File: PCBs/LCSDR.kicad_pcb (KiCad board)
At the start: 2 copper layers, 70 x 100 mm, 110 parts, among them CON2 AVR-ISP-6, J1 MIC, J10 SPK, J12 Conn_01x01, J13 Conn_01x01, J14 Conn_01x01, J15 Conn_01x01, J2 ANT, J3 USB_B, J4 CAL, J5 MEASURE, J6 I2C, J7 MEASURE, J8 Jack-DC, K1 TIANBO-HJR-4102-L, Q1 2N7002, Q2 2N7002, Q3 BC847, Q4 BS170, Q6 BS170, Q7 BF998, Q8 BS170, Q9 BC849, U1 74AC14, U2 Si5351, U3 FT232RL, U4 LM1117-5.0, U5 LM1117-3.3, U6 ATMEGA328P-AU, Y1 25Mhz, Y2 20Mhz

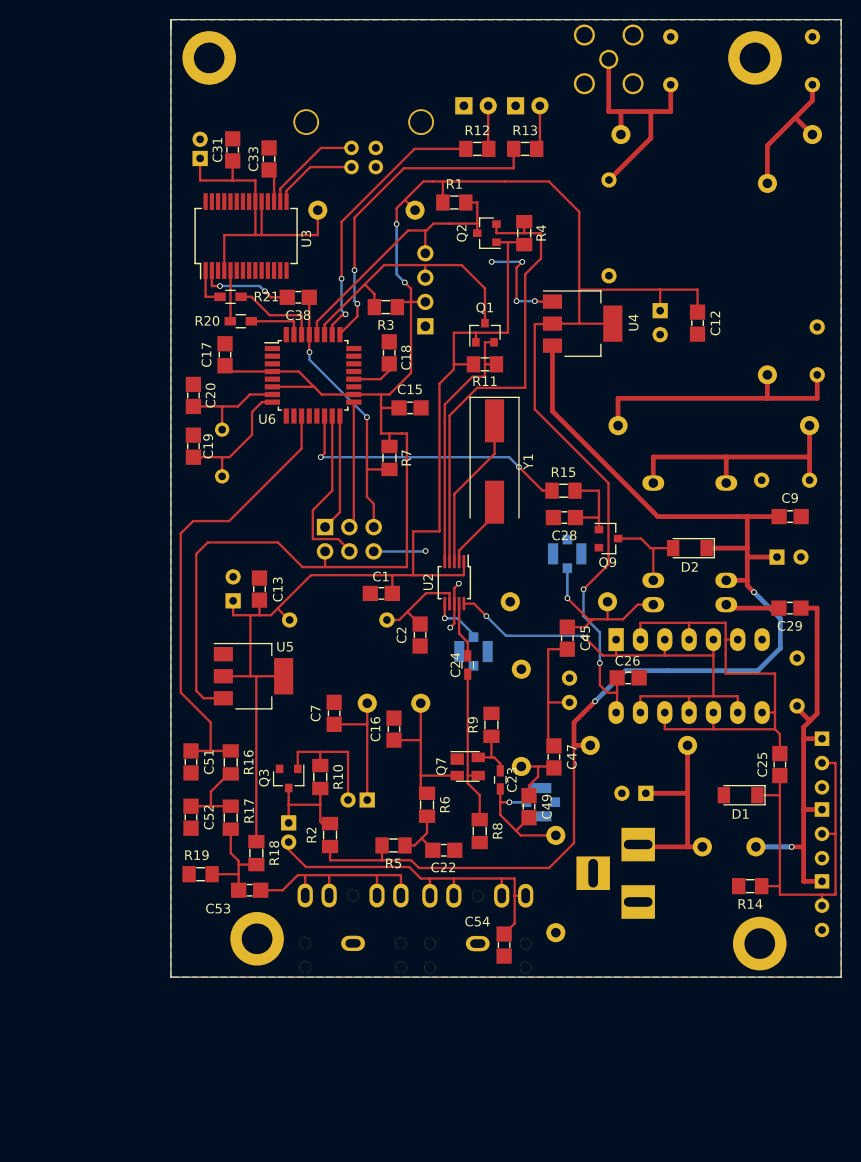
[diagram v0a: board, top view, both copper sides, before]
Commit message: ADX988 CAT: add FE, FI commands
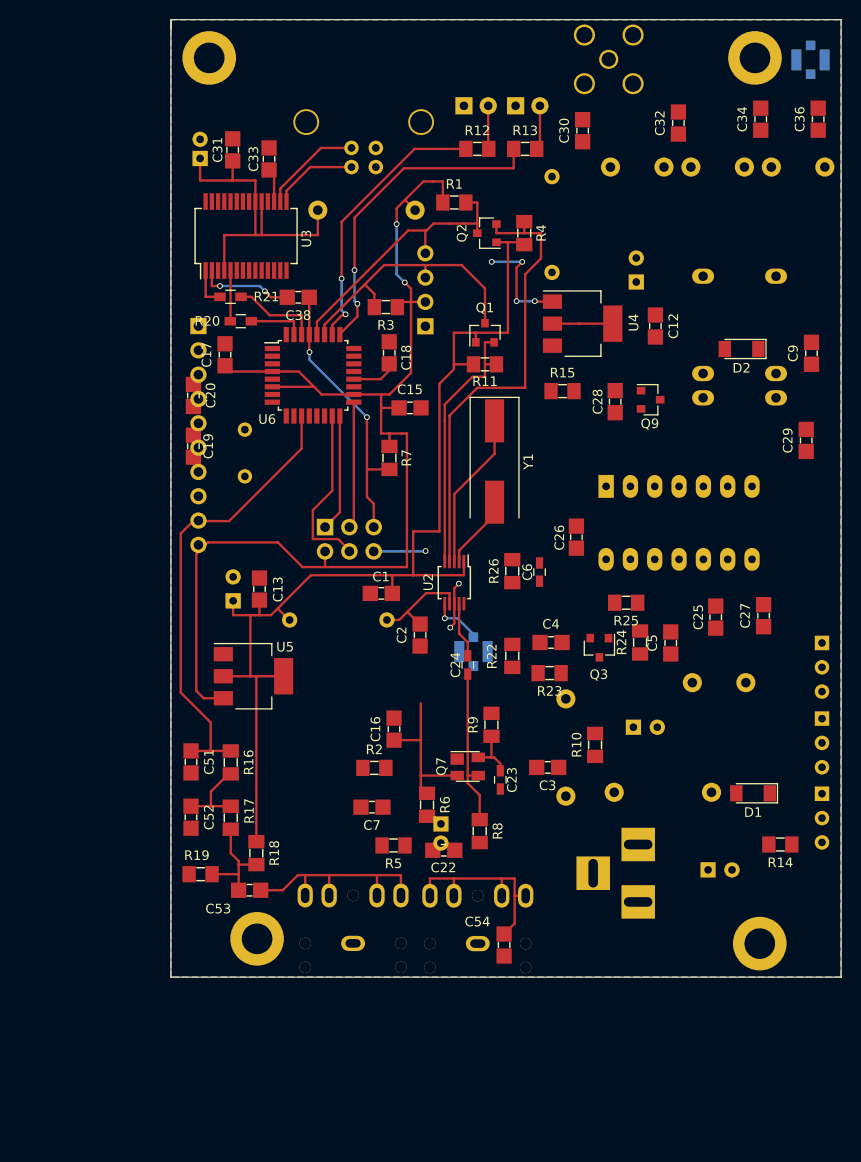
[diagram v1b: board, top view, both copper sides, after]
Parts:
- removed C45, C49: 330pF, LCSDR:C_1206_0603
- removed C47: 220pF, LCSDR:C_1206_0603
- removed L13, L19: 1uH, Choke_Axial_ThroughHole:Choke_Horizontal_RM10mm
- removed L15: 680nH, Resistors_THT:R_Axial_DIN0309_L9.0mm_D3.2mm_P2.54mm_Vertical
- removed L17: 680nH, Choke_Axial_ThroughHole:Choke_Horizontal_RM10mm
- removed L4: 100mH, Choke_Toroid_ThroughHole:Choke_Toroid_6,5x13mm_Vertical
- added C4: 100nF, LCSDR:C_1206_0603, F.Cu at (139.7, 125.0)
- added C5: 100nF, LCSDR:C_1206_0603, F.Cu at (152.2, 125.1)
- added C6: 10nF, Capacitors_SMD:C_0603_HandSoldering, F.Cu at (138.5, 117.7)
- added L3: 5.6uH, Choke_Axial_ThroughHole:Choke_Horizontal_RM10mm, B.Cu at (141.2, 136.1)
- added R22: 4.7, LCSDR:R_1206_0603, F.Cu at (135.7, 126.5)
- added R23: 47, LCSDR:R_1206_0603, F.Cu at (139.6, 128.2)
- added R24: 2.7K, LCSDR:R_1206_0603, F.Cu at (149.0, 125.0)
- added R25: 470, LCSDR:R_1206_0603, F.Cu at (147.6, 120.9)
- added R26: 1K, LCSDR:R_1206_0603, F.Cu at (135.7, 117.6)
- C16, C7: value 100nF -> 10nF
- C27: footprint Capacitors_THT:C_Disc_D4.7mm_W2.5mm_P5.00mm -> LCSDR:C_1206_0603; moved to F.Cu
- C3: value 2.2uF -> 100nF; footprint Capacitors_THT:CP_Radial_D5.0mm_P2.00mm -> LCSDR:C_1206_0603; moved to F.Cu
- C30, C36: value 270pF -> 360pF; footprint Capacitors_THT:C_Disc_D4.7mm_W2.5mm_P5.00mm -> LCSDR:C_1206_0603; moved to F.Cu
- C32, C34: value 680pF -> 750pF; footprint Capacitors_THT:C_Disc_D4.7mm_W2.5mm_P5.00mm -> LCSDR:C_1206_0603; moved to F.Cu
- J5: value MEASURE -> LPF
- J7: value MEASURE -> Conn_01x10; footprint LCSDR:U.FL_Molex_MCRF_73412-0110_Vertical -> Pin_Headers:Pin_Header_Straight_1x10_Pitch2.54mm
- L10, L6: value 1.32uH -> 1.22uH; footprint Choke_Axial_ThroughHole:Choke_Horizontal_RM20mm -> Choke_Toroid_ThroughHole:Choke_Toroid_6,5x13mm_Vertical
- L8: value 1.72uH -> 1.42uH; footprint Choke_Axial_ThroughHole:Choke_Horizontal_RM20mm -> Choke_Toroid_ThroughHole:Choke_Toroid_6,5x13mm_Vertical
- Q3: value BC847 -> BFR93A
- R10: value 470k -> 33
- R2: value 3.9K -> 2.2K
- moved J7 61.3 mm to (102.9, 92.0), turned to 180 degrees
- moved J5 57.5 mm to (166.8, 64.2), turned to 0 degrees
- moved C36 37.7 mm to (167.6, 70.4), turned to 90 degrees
- moved Q3 35.2 mm to (144.8, 125.6)
- moved R10 28.9 mm to (144.3, 135.8), turned to 90 degrees
- moved C3 27.7 mm to (139.3, 138.1), turned to 180 degrees
- moved C34 27.3 mm to (161.6, 70.4)
- moved C8 23.3 mm to (148.3, 133.9)
- moved K1 22.2 mm to (163.2, 86.8)
- moved D2 21.5 mm to (159.6, 94.4)
- moved L10 21.1 mm to (162.2, 82.0), turned to 90 degrees
- moved C29 17.6 mm to (166.3, 104.0), turned to 90 degrees
- moved C9 17.2 mm to (166.9, 94.8), turned to 90 degrees
- moved L5 17.2 mm to (153.9, 135.8)
- moved C25 16.8 mm to (156.9, 122.4)
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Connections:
- C23 pad 2: HPF -> Net-(C23-Pad2)
- C3 pad 2: Net-(C3-Pad2) -> GND
- C54 pad 1: Net-(C3-Pad2) -> Net-(C14-Pad2)
- J1 pad 2: Net-(C3-Pad2) -> Net-(C14-Pad2)
- J1 pad 3: Net-(C3-Pad2) -> Net-(C14-Pad2)
- J1 pad 4: Net-(C3-Pad2) -> Net-(C14-Pad2)
- J1 pad 5: Net-(C3-Pad2) -> Net-(C14-Pad2)
- J3 pad 1: (no net) -> Net-(J3-Pad1)
- J5 pad 1: RF_IN -> LPF
- J7 pad 1: HPF -> GND
- J7 pad 2: GND -> IO_4
- Q3 pad 1: Net-(C14-Pad2) -> Net-(C6-Pad1)
- Q3 pad 2: GND -> Net-(C4-Pad2)
- Q3 pad 3: Net-(C3-Pad1) -> Net-(C23-Pad2)
- R10 pad 1: Net-(C14-Pad2) -> Net-(C3-Pad1)
- R10 pad 2: Net-(C3-Pad1) -> +12V
- R2 pad 1: +12V -> Net-(C16-Pad1)
- R2 pad 2: Net-(C3-Pad1) -> Net-(C14-Pad1)
- U3 pad 10: (no net) -> Net-(U3-Pad10)
- U3 pad 11: (no net) -> Net-(U3-Pad11)
- U3 pad 12: (no net) -> Net-(U3-Pad12)
- U3 pad 13: (no net) -> Net-(U3-Pad13)
- U3 pad 14: (no net) -> Net-(U3-Pad14)
- U3 pad 22: (no net) -> Net-(U3-Pad22)
- U3 pad 23: (no net) -> Net-(U3-Pad23)
- U3 pad 27: (no net) -> Net-(U3-Pad27)
- U3 pad 28: (no net) -> Net-(U3-Pad28)
- U3 pad 3: (no net) -> Net-(U3-Pad3)
- U3 pad 6: (no net) -> Net-(U3-Pad6)
- U3 pad 9: (no net) -> Net-(U3-Pad9)
- U6 pad 1: (no net) -> IO_5
- U6 pad 12: (no net) -> IO_8
- U6 pad 13: (no net) -> IO_9
- U6 pad 14: RX_TX -> IO_10
- U6 pad 19: (no net) -> Net-(U6-Pad19)
- U6 pad 2: (no net) -> IO_6
- U6 pad 22: (no net) -> Net-(U6-Pad22)
- U6 pad 23: (no net) -> RX_TX
- U6 pad 24: (no net) -> IO_1
- U6 pad 32: (no net) -> IO_4
- U6 pad 9: (no net) -> IO_7
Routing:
- net +12V: track 128.7 -> 0.00 mm, vias 2 -> 0
- net +5V: track 224.0 -> 162.5 mm, vias 4 -> 2
- net CLK0: track 52.8 -> 0.00 mm, vias 2 -> 0
- net Net-(C25-Pad1): track 49.0 -> 0.00 mm
- net Net-(C27-Pad1): track 43.7 -> 0.00 mm, vias 1 -> 0
- net Net-(C25-Pad2): track 40.2 -> 0.00 mm
- net Net-(C3-Pad2): track 38.4 -> 0.00 mm
- net Net-(C51-Pad1): track 47.8 -> 14.9 mm
- net RX_TX: track 30.1 -> 0.00 mm, vias 2 -> 0
- net Net-(C34-Pad1): track 28.6 -> 0.00 mm
- net LPF: track 27.5 -> 0.00 mm
- net Net-(C30-Pad1): track 26.1 -> 0.00 mm
- net +12VA: track 21.8 -> 0.35 mm
- net RF_IN: track 18.5 -> 0.00 mm, vias 1 -> 0
- net Net-(C32-Pad1): track 14.8 -> 0.00 mm
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
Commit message: discret, simple, CH340E
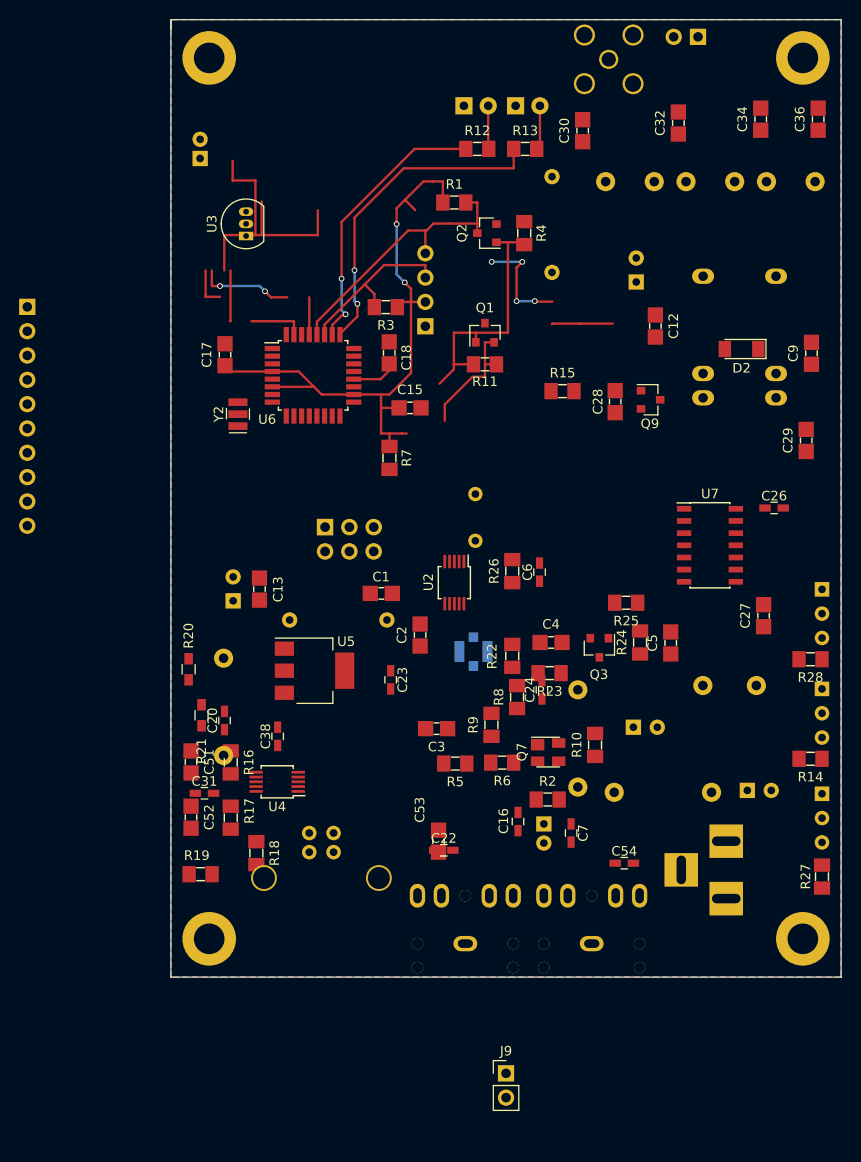
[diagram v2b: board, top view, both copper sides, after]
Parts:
- removed C19: 22pF, LCSDR:C_1206_0603
- removed C25, C33: 100nF, LCSDR:C_1206_0603
- removed D1: LL4148, Diodes_SMD:D_MiniMELF
- removed L12: 10uH, Choke_Axial_ThroughHole:Choke_Horizontal_RM10mm
- removed U1: 74AC14, Housings_DIP:DIP-14_W7.62mm_LongPads
- added J9: Conn_01x02, Pin_Headers:Pin_Header_Straight_1x02_Pitch2.54mm, F.Cu at (135.0, 170.1)
- added L4: 10uH, Choke_Axial_ThroughHole:Choke_Horizontal_RM10mm, B.Cu at (105.5, 131.8)
- added R27: 1R, LCSDR:R_1206_0603, F.Cu at (168.0, 149.5)
- added R28: 1R, LCSDR:R_1206_0603, F.Cu at (166.8, 126.8)
- added U7: 74ACT00, Housings_SOIC:SOIC-14_3.9x8.7mm_Pitch1.27mm, F.Cu at (156.3, 114.9)
- C16, C22, C26, C31, C38, C54, C7: footprint LCSDR:C_1206_0603 -> Capacitors_SMD:C_0603_HandSoldering
- C20: value 22pF -> 100nF; footprint LCSDR:C_1206_0603 -> Capacitors_SMD:C_0603_HandSoldering
- J5: value LPF -> Conn_01x02; footprint LCSDR:U.FL_Molex_MCRF_73412-0110_Vertical -> Pin_Headers:Pin_Header_Straight_1x02_Pitch2.54mm
- L10, L6, L8: footprint Choke_Toroid_ThroughHole:Choke_Toroid_6,5x13mm_Vertical -> Choke_Toroid_ThroughHole:Choke_Toroid_5x10mm_Vertical
- R14: value 2.7K -> 1R
- U3: value FT232RL -> L78L05_TO92; footprint Housings_SSOP:SSOP-28_5.3x10.2mm_Pitch0.65mm -> TO_SOT_Packages_THT:TO-92_Inline_Narrow_Oval
- U4: value LM1117-5.0 -> CH340E; footprint TO_SOT_Packages_SMD:SOT-223-3_TabPin2 -> Housings_SSOP:MSOP-10_3x3mm_Pitch0.5mm
- Y1: footprint Crystals:Crystal_SMD_HC49-SD -> Crystals:Crystal_HC49-U_Vertical; moved to B.Cu
- Y2: value 20Mhz -> 16Mhz; footprint Crystals:Crystal_HC49-U_Vertical -> LCSDR:Crystal_SMD_3213_3.2x1.3mm; moved to F.Cu
- moved J3 69.9 mm to (114.5, 144.9), turned to 270 degrees
- moved C31 67.3 mm to (103.5, 140.8), turned to 0 degrees
- moved U4 57.5 mm to (111.1, 139.6), turned to 180 degrees
- moved C38 45.9 mm to (111.2, 134.8), turned to 90 degrees
- moved R21 43.8 mm to (103.2, 132.7), turned to 90 degrees
- moved R20 36.8 mm to (101.8, 127.8), turned to 90 degrees
- moved C20 34.1 mm to (105.6, 133.2)
- moved C7 21.0 mm to (141.8, 144.9), turned to 270 degrees
- moved C26 20.9 mm to (163.0, 111.0), turned to 0 degrees
- moved C53 20.4 mm to (128.0, 145.8), turned to 90 degrees
- moved R2 18.4 mm to (139.3, 141.4)
- moved J7 18.0 mm to (85.0, 90.0)
- moved C16 16.2 mm to (136.2, 143.8), turned to 270 degrees
- moved C23 15.5 mm to (123.0, 128.9)
- moved C54 15.2 mm to (147.3, 148.1), turned to 0 degrees
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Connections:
- C31 pad 1: Net-(C31-Pad1) -> GND
- C31 pad 2: GND -> Net-(C31-Pad2)
- C38 pad 1: RESET -> Net-(C38-Pad1)
- C38 pad 2: Net-(C38-Pad2) -> RESET
- C44 pad 1: Net-(C31-Pad1) -> Net-(C20-Pad1)
- J3 pad 1: Net-(J3-Pad1) -> (no net)
- J5 pad 1: LPF -> Net-(C30-Pad1)
- Q1 pad 2: Net-(Q1-Pad2) -> SCL
- Q1 pad 3: SDA -> Net-(Q1-Pad3)
- Q2 pad 2: Net-(Q2-Pad2) -> SDA
- Q2 pad 3: SCL -> Net-(Q2-Pad3)
- Q4 pad 2: Net-(C25-Pad2) -> Net-(Q4-Pad2)
- Q4 pad 3: GND -> Net-(Q4-Pad3)
- Q6 pad 2: Net-(C25-Pad2) -> Net-(Q4-Pad2)
- Q6 pad 3: GND -> Net-(Q6-Pad3)
- Q8 pad 2: Net-(C25-Pad2) -> Net-(Q4-Pad2)
- Q8 pad 3: GND -> Net-(Q8-Pad3)
- R11 pad 2: Net-(Q1-Pad2) -> Net-(Q2-Pad3)
- R14 pad 1: Net-(C25-Pad2) -> Net-(Q4-Pad3)
- R20 pad 1: TxD -> Net-(R20-Pad1)
- R20 pad 2: Net-(R20-Pad2) -> TxD
- R21 pad 1: RxD -> Net-(R21-Pad1)
- R21 pad 2: Net-(R21-Pad2) -> RxD
- R4 pad 2: Net-(Q2-Pad2) -> Net-(Q1-Pad3)
- U2 pad 4: Net-(Q2-Pad2) -> Net-(Q1-Pad3)
- U2 pad 5: Net-(Q1-Pad2) -> Net-(Q2-Pad3)
- U3 pad 1: Net-(R21-Pad2) -> +5V
- U3 pad 2: Net-(C38-Pad2) -> GND
- U3 pad 3: Net-(U3-Pad3) -> +12V
- U4 pad 1: GND -> Net-(J3-Pad3)
- U4 pad 2: +5V -> Net-(J3-Pad2)
- U4 pad 3: +12V -> GND
- U5 pad 3: +5V -> +12V
- U6 pad 19: Net-(U6-Pad19) -> (no net)
- U6 pad 22: Net-(U6-Pad22) -> (no net)
- U6 pad 24: IO_1 -> (no net)
- U6 pad 7: Net-(C20-Pad1) -> Net-(U6-Pad7)
- Y2 pad 2: Net-(C20-Pad1) -> GND
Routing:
- net +5V: track 162.5 -> 66.6 mm
- net +3V3: track 113.9 -> 27.2 mm
- net (no net): track 0.00 -> 67.1 mm, vias 0 -> 6
- net Net-(Q2-Pad2): track 48.0 -> 0.00 mm
- net Net-(C31-Pad1): track 35.4 -> 0.00 mm
- net Net-(Q1-Pad2): track 27.6 -> 0.00 mm
- net RESET: track 29.1 -> 3.90 mm, vias 2 -> 0
- net Net-(C53-Pad1): track 23.8 -> 0.00 mm
- net GND: track 21.9 -> 0.00 mm, vias 7 -> 0
- net Net-(C14-Pad2): track 21.7 -> 0.00 mm
- net Net-(U2-Pad3): track 19.2 -> 0.00 mm
- net Net-(CON2-Pad4): track 18.1 -> 0.00 mm
- net Net-(C24-Pad1): track 16.8 -> 0.00 mm
- net Net-(C16-Pad1): track 16.3 -> 0.00 mm
- net Net-(C51-Pad1): track 14.9 -> 0.00 mm
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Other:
- net class Default: trace_width 0.25 -> 0.2

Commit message: INIT project, si5351 generate properly frequency
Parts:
- removed C17, C18: 100nF, LCSDR:C_1206_0603
- removed C20, C31, C38: 100nF, Capacitors_SMD:C_0603_HandSoldering
- removed C44: 10uF, Capacitors_THT:CP_Radial_D5.0mm_P2.00mm
- removed CON2: AVR-ISP-6, Connectors_IDC:IDC-Header_2x03_Pitch2.54mm_Straight
- removed J3: USB_B, Connectors:USB_B
- removed J6: I2C, Pin_Headers:Pin_Header_Straight_1x04_Pitch2.54mm
- removed L4: 10uH, Choke_Axial_ThroughHole:Choke_Horizontal_RM10mm
- removed R20, R21: 1K, Resistors_SMD:R_0603_HandSoldering
- removed R7: 10k, LCSDR:R_1206_0603
- removed U3: L78L05_TO92, TO_SOT_Packages_THT:TO-92_Inline_Narrow_Oval
- removed U4: CH340E, Housings_SSOP:MSOP-10_3x3mm_Pitch0.5mm
- removed Y2: 16Mhz, LCSDR:Crystal_SMD_3213_3.2x1.3mm
- added U1: 24LC01, Housings_SOIC:SOIC-8_3.9x4.9mm_Pitch1.27mm, F.Cu at (115.9, 154.3)
- C12, C13, C15, C29, C3, C30, C32, C34, C36, C4, C5, C51, C52, C9: footprint LCSDR:C_1206_0603 -> Capacitors_SMD:C_0603_HandSoldering
- C27: value 100pF -> 100nF; footprint LCSDR:C_1206_0603 -> Capacitors_SMD:C_0603_HandSoldering
- C28: value 100pF -> 15nF; footprint LCSDR:C_1206_0603 -> Capacitors_SMD:C_0603_HandSoldering
- C53: value 100nF -> 1uF; footprint LCSDR:C_1206_0603 -> Capacitors_SMD:C_0603_HandSoldering
- D3, D4: footprint LEDs:LED_D3.0mm_Horizontal_O3.81mm_Z10.0mm -> LEDs:LED_0603_HandSoldering
- J9: moved to B.Cu
- L1: footprint Resistors_THT:R_Axial_DIN0207_L6.3mm_D2.5mm_P10.16mm_Horizontal -> Choke_Axial_ThroughHole:Choke_Horizontal_RM10mm
- L10, L6: value 1.22uH -> 1.42uH
- L8: value 1.42uH -> 1.62uH
- R1, R11, R15, R16, R17, R18, R19, R3, R4: footprint LCSDR:R_1206_0603 -> Resistors_SMD:R_0603_HandSoldering
- R12, R13: footprint LCSDR:R_1206_0603 -> Resistors_SMD:R_0603_HandSoldering; moved to B.Cu
- U6: value ATMEGA328P-AU -> Arduino_Nano; footprint Housings_QFP:TQFP-32_7x7mm_Pitch0.8mm -> Arduino:Arduino_Nano; moved to B.Cu
- moved J9 69.6 mm to (141.5, 100.8), turned to 270 degrees
- moved J7 62.1 mm to (102.6, 149.6), turned to 0 degrees
- moved Q2 59.5 mm to (117.0, 139.7), turned to 0 degrees
- moved C15 58.5 mm to (114.2, 158.1)
- moved C10 56.6 mm to (103.6, 121.8)
- moved C12 56.4 mm to (106.6, 127.2), turned to 90 degrees
- moved R1 55.1 mm to (113.8, 131.9)
- moved R4 48.7 mm to (118.3, 127.3), turned to 0 degrees
- moved J2 47.2 mm to (119.0, 103.2)
- moved J5 47.2 mm to (128.5, 100.8)
- moved R3 46.8 mm to (113.1, 135.8), turned to 270 degrees
- moved E1 45.3 mm to (111.4, 111.7), turned to 180 degrees
- moved C30 43.9 mm to (124.7, 111.5), turned to 0 degrees
- moved R11 43.8 mm to (117.0, 136.8)
- moved R13 41.6 mm to (108.7, 104.0), turned to 90 degrees
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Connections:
- C51 pad 1: Net-(C51-Pad1) -> AUDIO_IN
- R16 pad 1: Net-(C51-Pad1) -> AUDIO_IN
- U6 pad 1: IO_5 -> (no net)
- U6 pad 10: GND -> AUDIO_IN
- U6 pad 11: Net-(C51-Pad1) -> IO_6
- U6 pad 12: IO_8 -> IO_5
- U6 pad 13: IO_9 -> IO_4
- U6 pad 14: IO_10 -> (no net)
- U6 pad 15: Net-(CON2-Pad4) -> (no net)
- U6 pad 16: Net-(CON2-Pad1) -> (no net)
- U6 pad 17: Net-(CON2-Pad3) -> (no net)
- U6 pad 18: +5V -> (no net)
- U6 pad 19: (no net) -> IO_7
- U6 pad 2: IO_6 -> (no net)
- U6 pad 20: Net-(C18-Pad1) -> IO_8
- U6 pad 21: GND -> IO_9
- U6 pad 22: (no net) -> IO_10
- U6 pad 23: RX_TX -> SDA
- U6 pad 24: (no net) -> SCL
- U6 pad 25: LED_RED -> AUDIO_IN
- U6 pad 26: LED_GREEN -> AUDIO_IN
- U6 pad 27: SDA -> +5V
- U6 pad 28: SCL -> (no net)
- U6 pad 29: RESET -> GND
- U6 pad 3: GND -> (no net)
- U6 pad 30: RxD -> +12V
- U6 pad 4: +5V -> GND
- U6 pad 5: GND -> RX_TX
- U6 pad 6: +5V -> RX_TX_PA
- U6 pad 7: Net-(U6-Pad7) -> LED_GREEN
- U6 pad 8: Net-(U6-Pad8) -> LED_RED
- U6 pad 9: IO_7 -> GND
- U7 pad 2: RX_TX -> RX_TX_PA
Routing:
- net +12V: track 0.00 -> 127.0 mm, vias 0 -> 2
- net +5V: track 66.6 -> 142.3 mm
- net (no net): track 67.1 -> 0.00 mm, vias 6 -> 0
- net GND: track 0.00 -> 53.6 mm, vias 0 -> 13
- net +3V3: track 27.2 -> 80.0 mm, vias 0 -> 4
- net Net-(Q4-Pad2): track 0.00 -> 44.4 mm, vias 0 -> 1
- net RX_TX_PA: track 0.00 -> 42.9 mm, vias 0 -> 1
- net Net-(C27-Pad1): track 0.00 -> 40.2 mm
- net Net-(Q2-Pad3): track 2.20 -> 37.8 mm
- net Net-(C30-Pad1): track 0.00 -> 34.9 mm
- net RX_TX: track 0.00 -> 34.0 mm, vias 0 -> 2
- net AUDIO_IN: track 0.00 -> 32.8 mm, vias 0 -> 2
- net Net-(Q1-Pad3): track 0.00 -> 29.8 mm
- net CLK0: track 0.00 -> 28.3 mm
- net +12VA: track 0.00 -> 23.9 mm
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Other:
- board size 70 x 100 mm -> 70 x 61 mm
- net class Default: trace_width 0.2 -> 0.5

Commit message: add printout, finish PCB, add LM7805
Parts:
- removed J4: CAL, LCSDR:U.FL_Molex_MCRF_73412-0110_Vertical
- added J3: Calibration, Pin_Headers:Pin_Header_Straight_1x02_Pitch2.54mm, B.Cu at (130.3, 130.3)
- added R7: 0, Resistors_SMD:R_0603_HandSoldering, F.Cu at (110.8, 127.1)
- added U3: L7805, TO_SOT_Packages_THT:TO-220-3_Vertical, B.Cu at (167.2, 114.4)
- moved C13 14.6 mm to (121.5, 115.3), turned to 90 degrees
- moved C12 12.4 mm to (104.7, 115.0), turned to 135 degrees
- moved C29 10.0 mm to (161.2, 104.8)
- moved C30 5.97 mm to (126.6, 105.8), turned to 90 degrees
- moved R27 5.23 mm to (164.0, 147.2), turned to 180 degrees
- moved C27 3.97 mm to (160.3, 133.6), turned to 180 degrees
- moved C9 3.84 mm to (134.4, 111.4)
- moved R1 2.06 mm to (114.2, 129.9), turned to 270 degrees
- moved R4 1.54 mm to (119.2, 126.1), turned to 270 degrees
- moved C3 1.38 mm to (139.2, 115.3)
- moved R14 1.18 mm to (166.8, 138.2), turned to 180 degrees
- moved C26 1.12 mm to (162.3, 113.5)
- moved R28 1.10 mm to (168.0, 127.2)
- moved Q4 1.00 mm to (168.0, 130.9)
- moved Q8 1.00 mm to (168.0, 118.7)
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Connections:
- U5 pad 3: +12V -> +5V
- U6 pad 27: +5V -> Net-(R7-Pad1)
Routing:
- net GND: track 53.6 -> 128.4 mm, vias 13 -> 27
- net Net-(C27-Pad1): track 40.2 -> 62.0 mm
- net +12V: track 127.0 -> 143.3 mm, vias 2 -> 4
- net +5V: track 142.3 -> 152.5 mm
- net Net-(C29-Pad2): track 13.5 -> 3.30 mm
- net RX_TX: track 34.0 -> 39.4 mm, vias 2 -> 1
- net +3V3: track 80.0 -> 83.5 mm
- net Net-(C30-Pad1): track 34.9 -> 31.7 mm
- net Net-(R7-Pad1): track 0.00 -> 2.17 mm
- net Net-(Q4-Pad2): track 44.4 -> 46.5 mm
- net SCL: track 34.9 -> 36.3 mm
- net Net-(C3-Pad1): track 8.30 -> 9.30 mm
- net Net-(Q6-Pad3): track 2.17 -> 2.80 mm
- net Net-(C6-Pad1): track 20.9 -> 21.4 mm
- net RX_TX_PA: track 42.9 -> 43.4 mm
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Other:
- net class Default: trace_width 0.5 -> 0.25
